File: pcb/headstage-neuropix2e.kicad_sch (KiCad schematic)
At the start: 5 parts, among them J1 X.FL-R-SMT-1

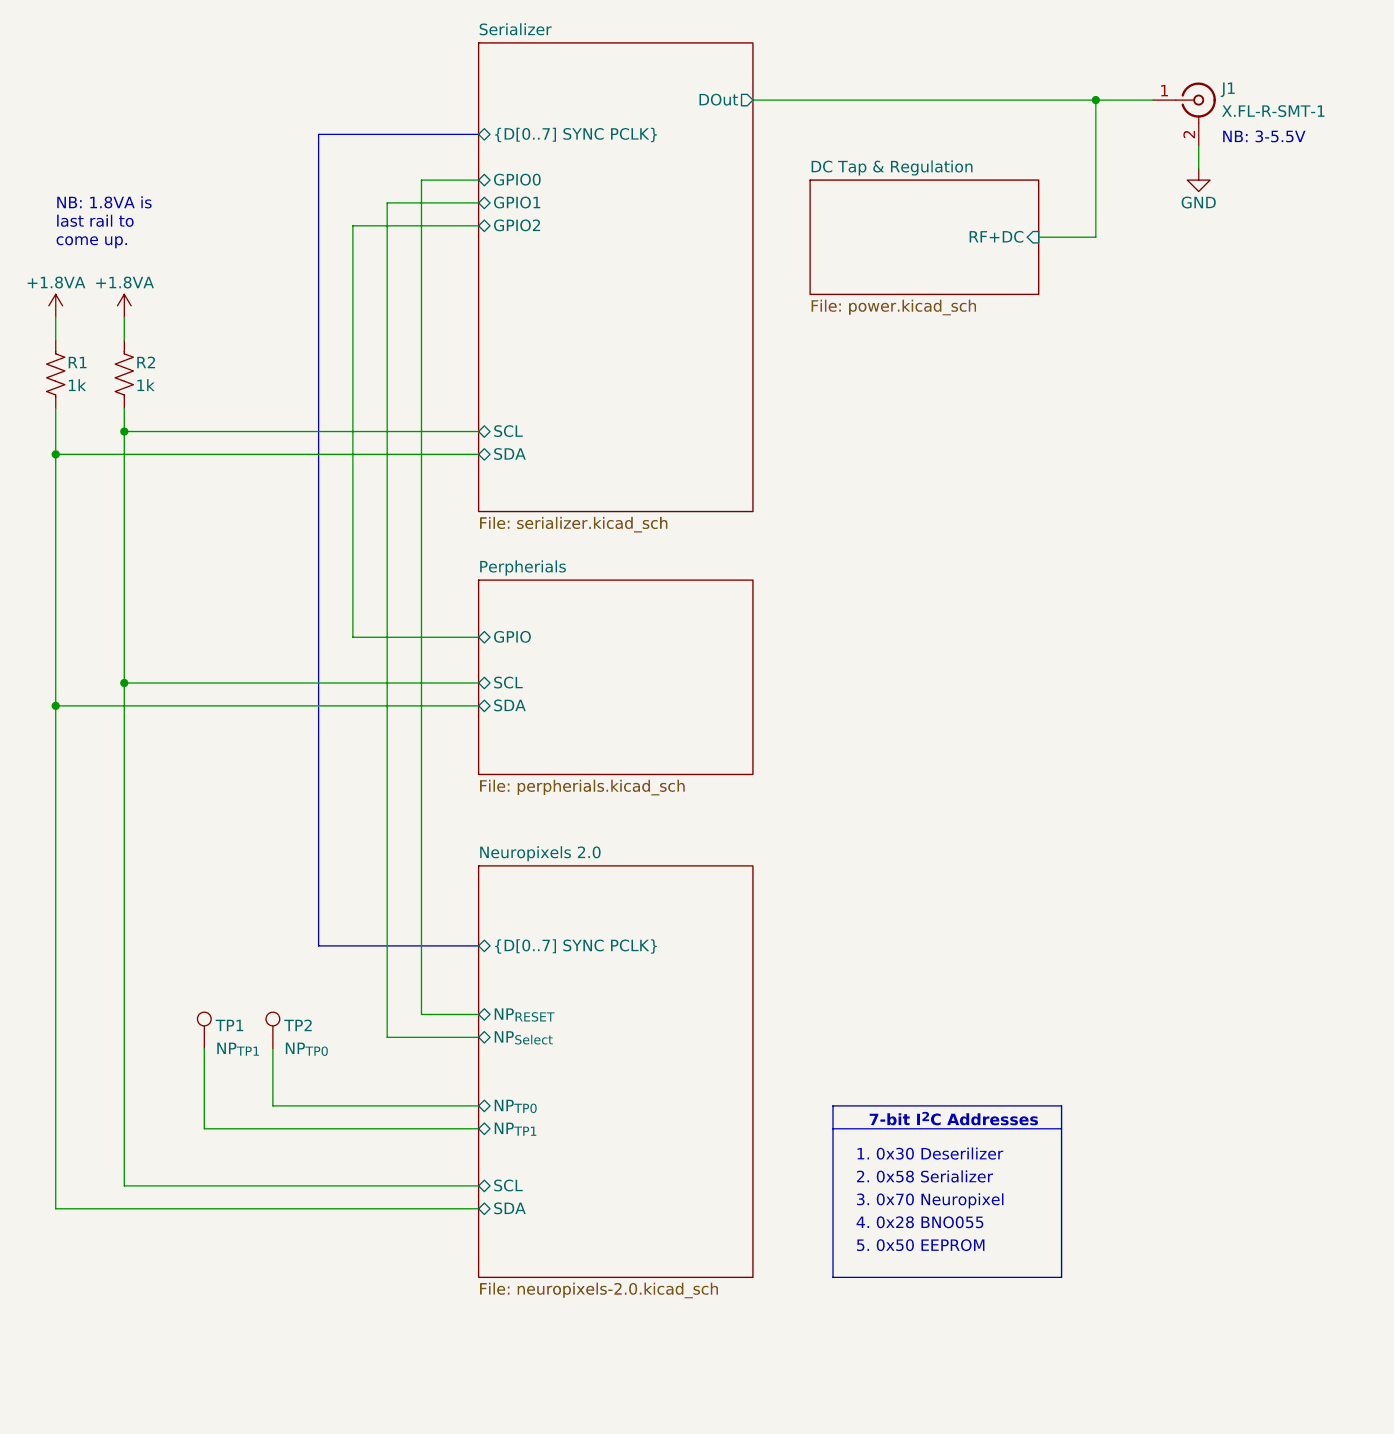
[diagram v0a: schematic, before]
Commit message: Inital routing complete
- Addressed Aaron's review
- Pullup on output side of analog switch to prevent floating SDA
- Other minor changes
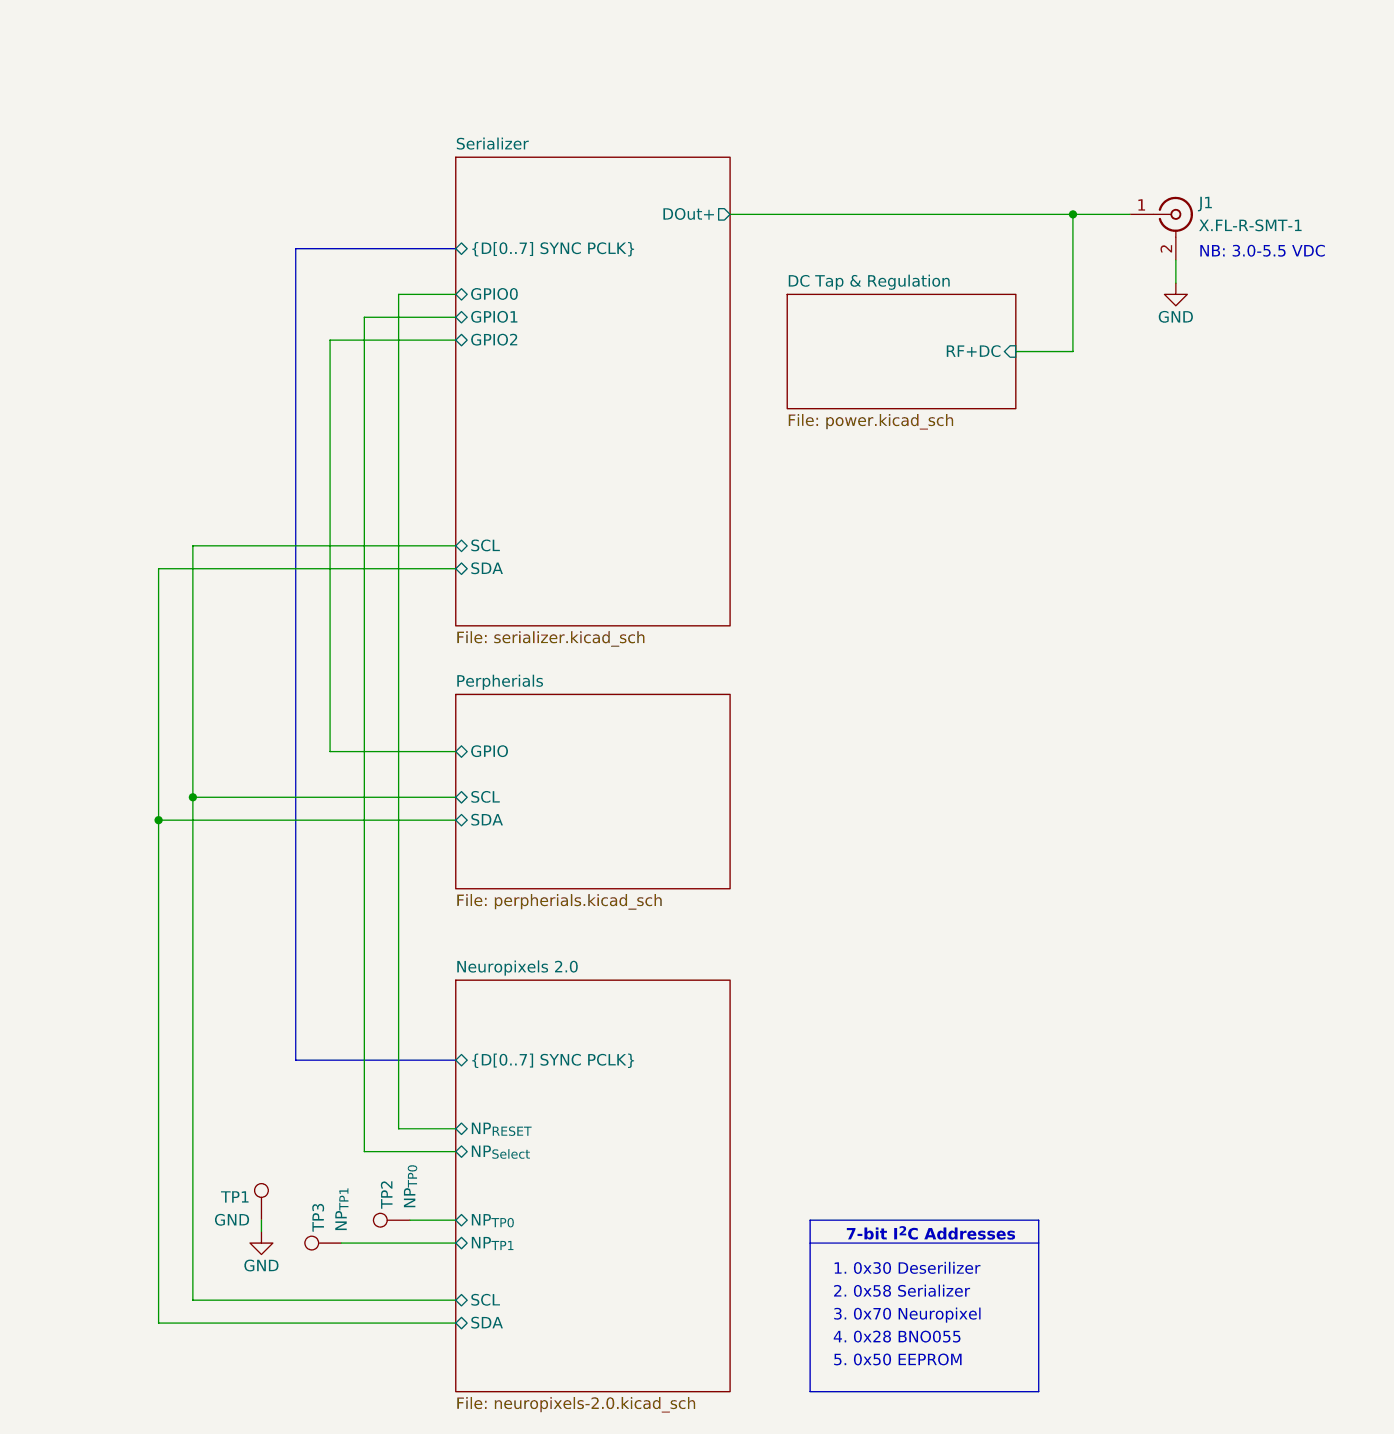
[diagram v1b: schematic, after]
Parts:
- removed R1, R2: 1k, Resistor_SMD:R_0201_0603Metric, symbol Device:R_US
- added TP1: GND, jonnew:OE_TP-Oval-2.8x1.6mm, symbol Connector:TestPoint
- TP2: footprint TestPoint:TestPoint_THTPad_D3.0mm_Drill1.5mm -> jonnew:OE_TP-Oval-2.8x1.6mm
- renumbered TP1 to TP3
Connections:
- net GND: now also TP1.1
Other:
- sheet Serializer ports: added DOut+; removed DOut
- note added: "NB: 3.0-5.5 VDC"
- note removed: "NB: 1.8VA is last rail to come up."
- note removed: "NB: 3-5.5V"
- moved on the sheet: J1, TP2, TP3

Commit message: Address team comments
- Add extra mouse-bite supports
- Enbiggen cable strain relief spear
- Add DNP 0.1" header for bench debug
- Small routing changes
- Update and complete BOM
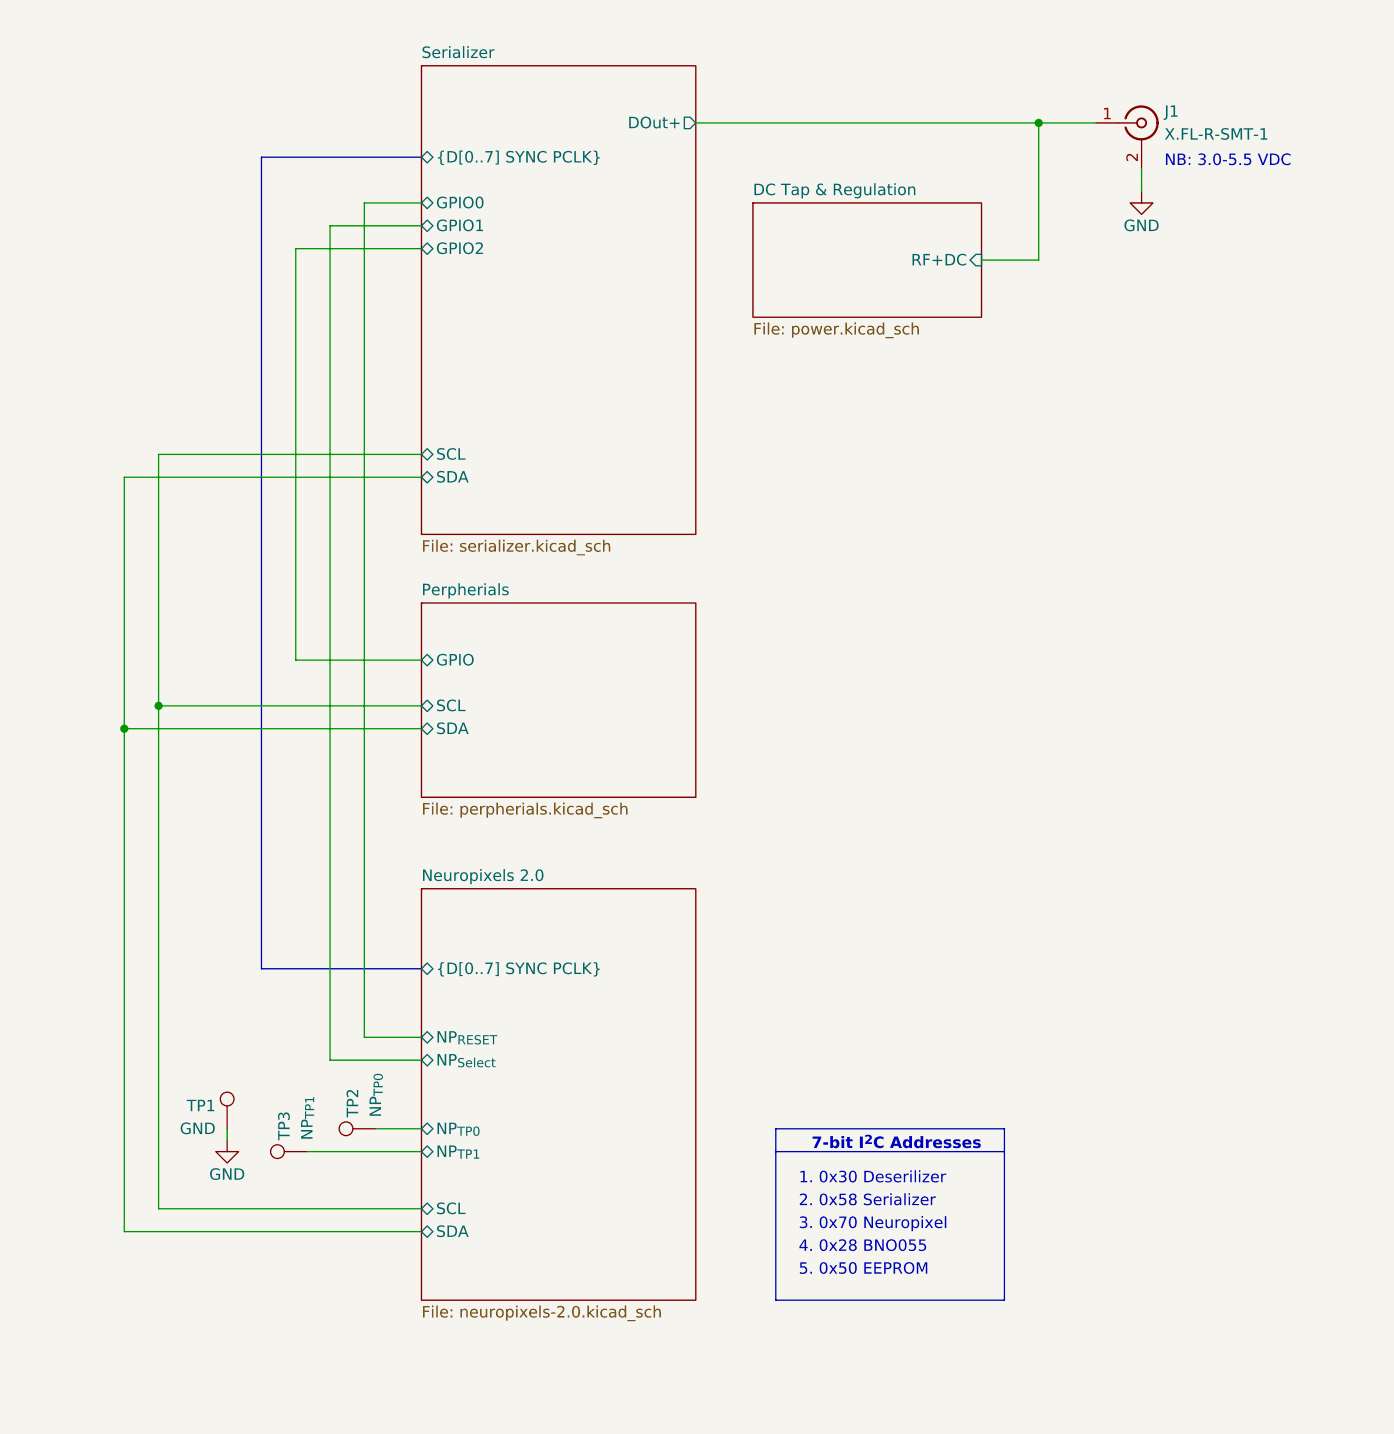
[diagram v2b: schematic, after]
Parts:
- J1, TP1, TP2, TP3: DNP DNP -> (none)
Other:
- moved on the sheet: J1, TP1, TP2, TP3

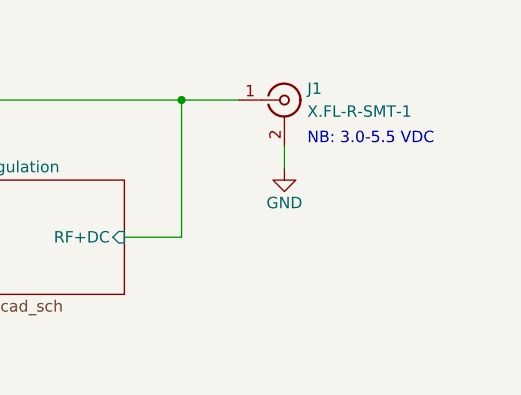
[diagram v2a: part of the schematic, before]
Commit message: Updates to design after feedback from assembler
- Replace obsolete TE_2013496-9 ZIF connector used by IMEC with
046844727002846+, which should fit NP 2.0 flex connectors (see design
folder for comparison). We will see.
- Replaced programmable MEMS oscillator with standard quartz since this
is a common frequency.
- Other BOM updates to account for obsolete or out of stock components
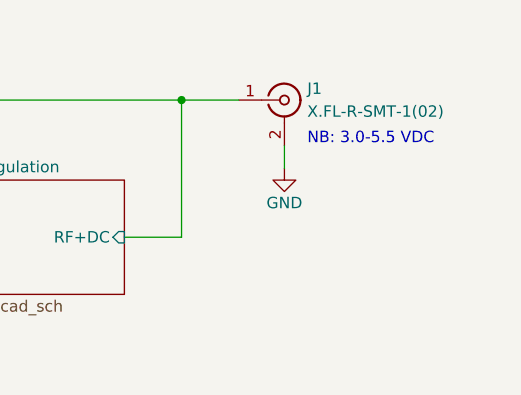
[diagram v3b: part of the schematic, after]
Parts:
- J1: value X.FL-R-SMT-1 -> X.FL-R-SMT-1(02)
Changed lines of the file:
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@@
       (effects (font (size 1.27 1.27)) (justify left))
     )
-    (property "Value" "X.FL-R-SMT-1" (at 165.1 83.82 0)
+    (property "Value" "X.FL-R-SMT-1(02)" (at 165.1 83.82 0)
       (effects (font (size 1.27 1.27)) (justify left))
     )
